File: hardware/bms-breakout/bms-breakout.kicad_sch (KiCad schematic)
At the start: 16 parts, among them J1 IN-A, J10 V-SUPP, J11 Smol_Brain_Board, J12 DE9_Socket_MountingHoles, J13 UART_CONN, J14 BMS_SW, J15 SBB_POWER, J2 IN-B, J3 IN-C, J4 BALANCE-A, J5 BALANCE-B, J6 BALANCE-C, J7 Conn_01x23, J8 BMS-OUT, J9 BMS-IN

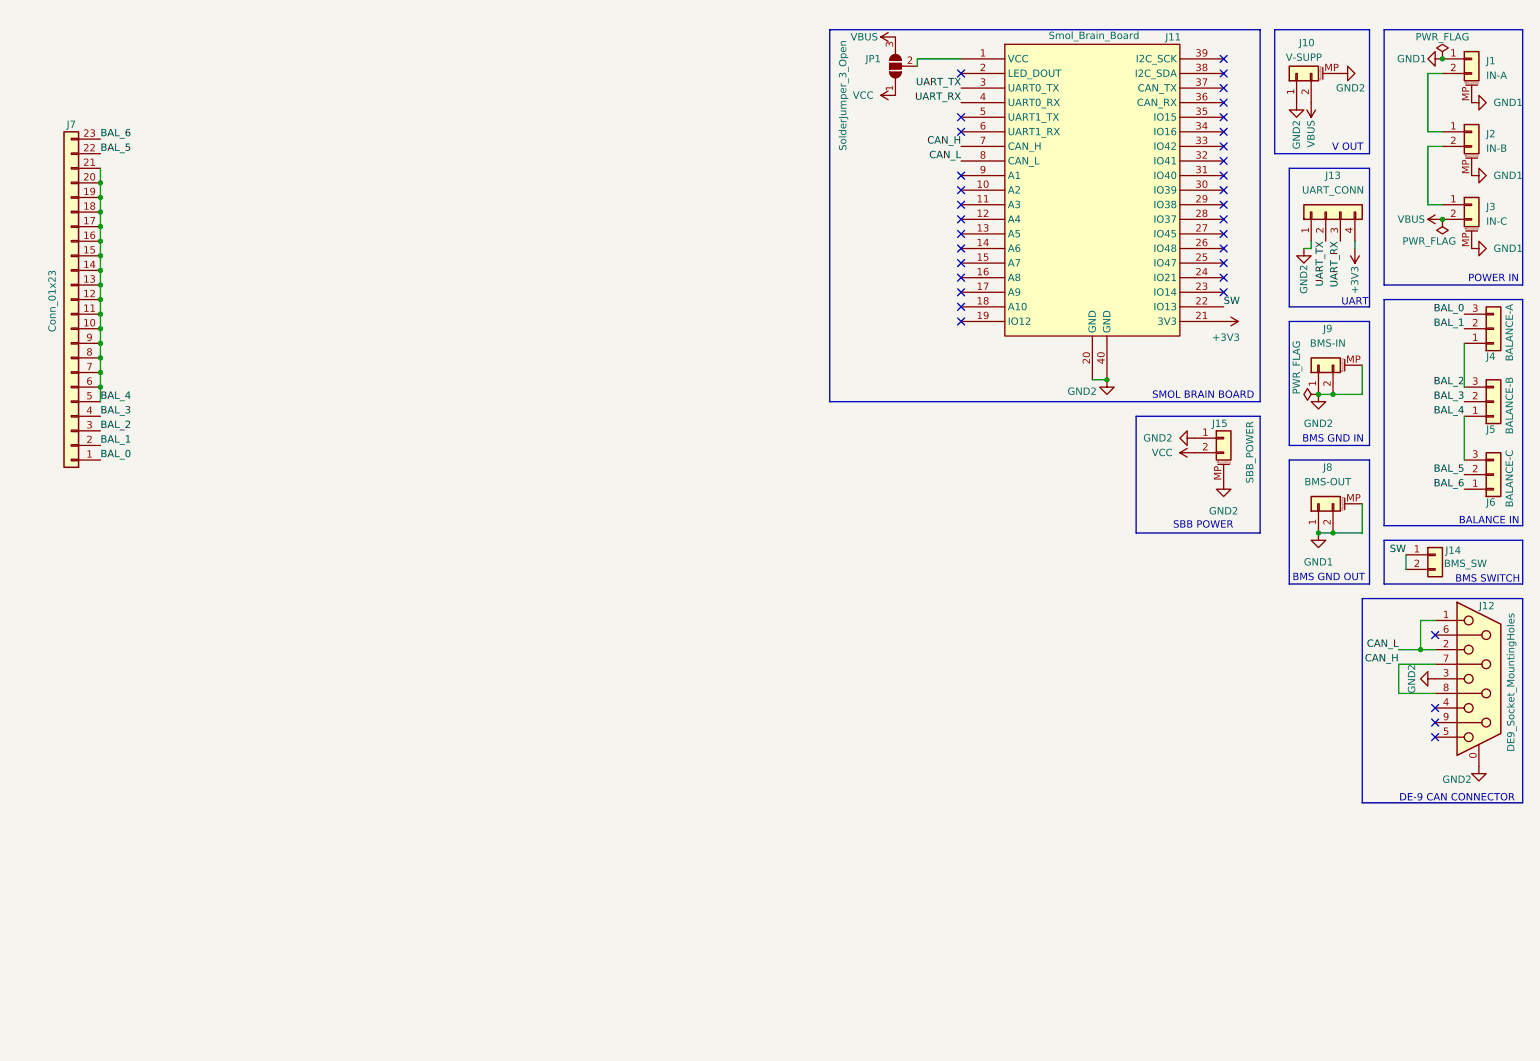
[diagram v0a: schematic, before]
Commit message: Updated Schematic
- Changed Layout
- Added Estop fet for discharge switch
- Added voltage balance connectors
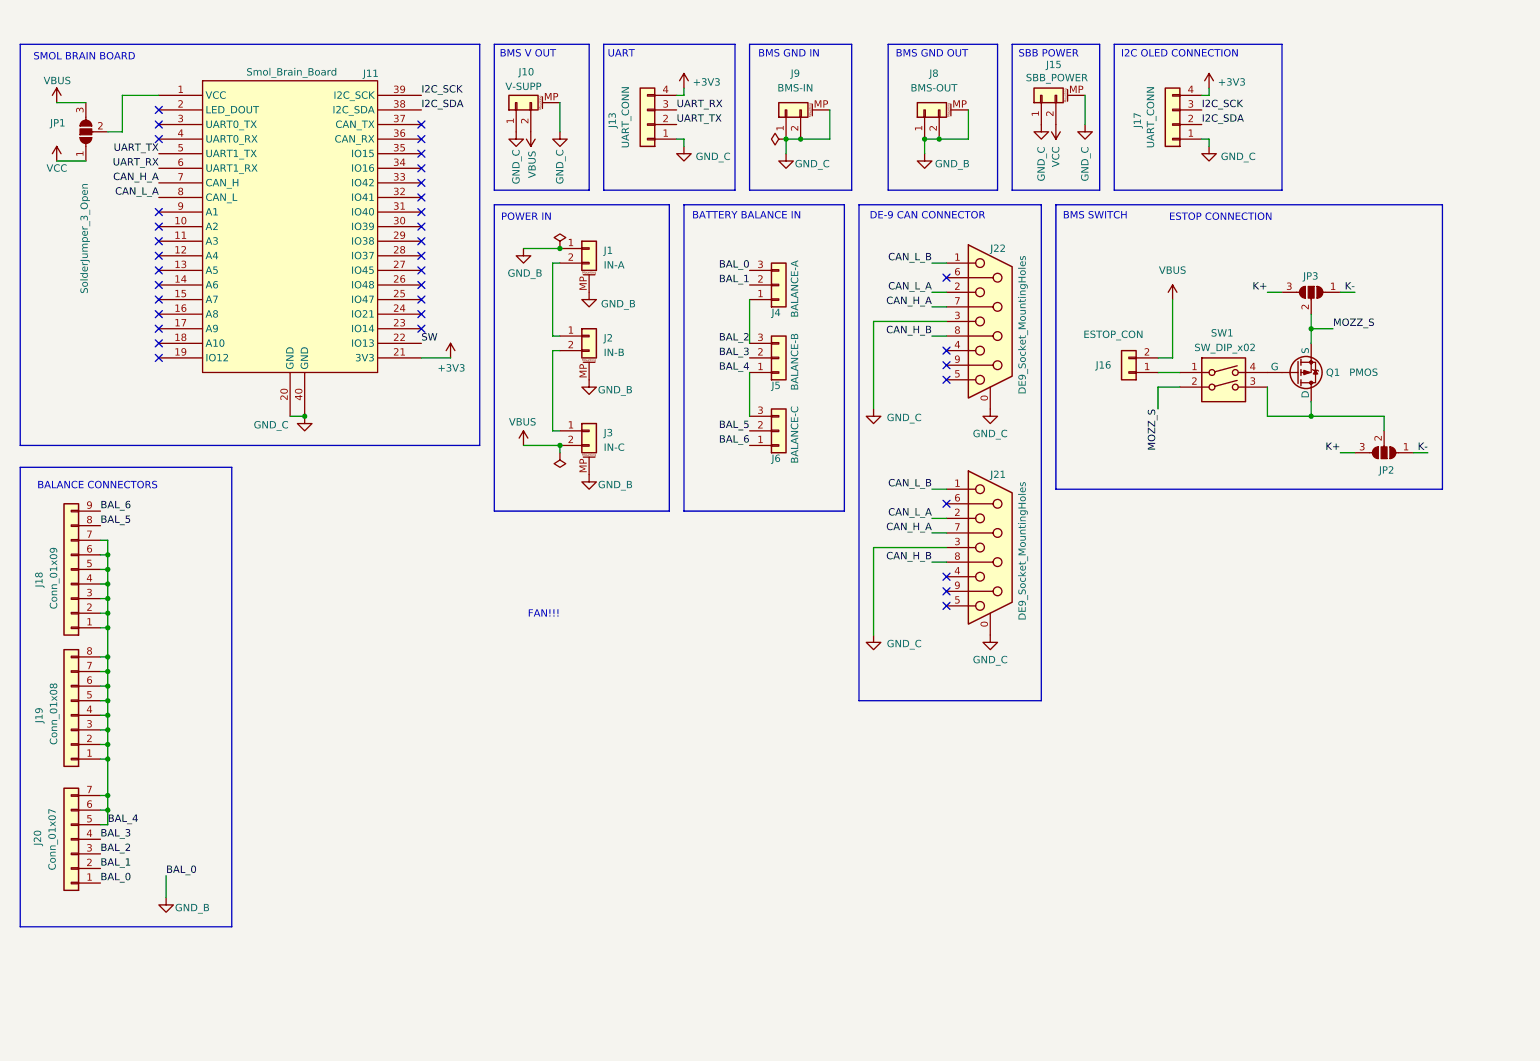
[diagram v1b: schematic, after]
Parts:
- removed J12: DE9_Socket_MountingHoles, Connector_Dsub:DSUB-9_Socket_Horizontal_P2.77x2.84mm_EdgePinOffset4.94mm_Housed_MountingHolesOffset4.94mm, symbol Connector:DE9_Socket_MountingHoles
- removed J14: BMS_SW, symbol Connector_Generic:Conn_01x02
- removed J7: Conn_01x23, symbol Connector_Generic:Conn_01x23
- added J16: ESTOP_CON, symbol Connector_Generic:Conn_01x02
- added J17: UART_CONN, Connector_JST:JST_XH_S4B-XH-A-1_1x04_P2.50mm_Horizontal, symbol Connector_Generic:Conn_01x04
- added J18: Conn_01x09, symbol Connector_Generic:Conn_01x09
- added J19: Conn_01x08, symbol Connector_Generic:Conn_01x08
- added J20: Conn_01x07, symbol Connector_Generic:Conn_01x07
- added J21, J22: DE9_Socket_MountingHoles, Connector_Dsub:DSUB-9_Socket_Horizontal_P2.77x2.84mm_EdgePinOffset4.94mm_Housed_MountingHolesOffset4.94mm, symbol Connector:DE9_Socket_MountingHoles
- added JP2, JP3: SolderJumper_3_Open, Jumper:SolderJumper-3_P2.0mm_Open_TrianglePad1.0x1.5mm, symbol Jumper:SolderJumper_3_Open
- added Q1: PMOS, symbol Simulation_SPICE:PMOS
- added SW1: SW_DIP_x02, symbol Switch:SW_DIP_x02
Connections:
- net GND1 is gone; now on net GND_B: J1.1 (Pin_1), J1.MP (MountPin), J2.MP (MountPin), J3.MP (MountPin), J8.1 (Pin_1), J8.2 (Pin_2), J8.MP (MountPin)
- net +3V3: now also J17.4 (Pin_4)
- net BAL_1: now also J20.2 (Pin_2)
- net BAL_2: now also J20.3 (Pin_3)
- net BAL_3: now also J20.4 (Pin_4)
- net BAL_4: now also J18.1 (Pin_1), J18.2 (Pin_2), J18.3 (Pin_3), J18.4 (Pin_4), J18.5 (Pin_5), J18.6 (Pin_6), J18.7 (Pin_7), J19.1 (Pin_1), J19.2 (Pin_2), J19.3 (Pin_3), J19.4 (Pin_4), J19.5 (Pin_5), J19.6 (Pin_6), J19.7 (Pin_7), J19.8 (Pin_8), J20.5 (Pin_5), J20.6 (Pin_6), J20.7 (Pin_7)
- net BAL_5: now also J18.8 (Pin_8)
- net BAL_6: now also J18.9 (Pin_9)
- net UART_RX: now also J11.6 (UART1_RX); no longer J11.4 (UART0_RX)
- net UART_TX: now also J11.5 (UART1_TX); no longer J11.3 (UART0_TX)
- net VBUS: now also J16.2 (Pin_2)
- net I2C_SDA: now reaches J11.38 (I2C_SDA)
- net I2C_SDA: now also J17.2 (Pin_2)
- net I2C_SCK: now reaches J11.39 (I2C_SCK)
- net I2C_SCK: now also J17.3 (Pin_3)
- net BAL_0 renamed GND_B
- net GND_B: now also J20.1 (Pin_1)
- net CAN_H renamed CAN_H_A
- net CAN_H_A: now also J21.7, J22.7
- net CAN_L renamed CAN_L_A
- net CAN_L_A: now also J21.2, J22.2
- net GND2 renamed GND_C
- net GND_C: now also J17.1 (Pin_1), J21.0 (PAD), J21.3, J22.0 (PAD), J22.3
- new net: J16.1 (Pin_1), SW1.1
- new net: JP2.2 (C), Q1.1 (D), SW1.3
- new net: Q1.2 (G), SW1.4
- new net CAN_H_B: J21.8, J22.8
- new net CAN_L_B: J21.1, J22.1
- new net K+: JP2.3 (B), JP3.3 (B)
- new net K-: JP2.1 (A), JP3.1 (A)
- new net MOZZ_S: JP3.2 (C), Q1.3 (S), SW1.2
- no-connect marks 35 -> 37
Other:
- note added: "BALANCE CONNECTORS"
- note added: "BATTERY BALANCE IN"
- note added: "BMS V OUT"
- note added: "ESTOP CONNECTION"
- note added: "FAN!!!"
- note added: "I2C OLED CONNECTION"
- note removed: "BALANCE IN"
- note removed: "V OUT"
- moved on the sheet: J1, J10, J11, J13, J15, J2, J3, J4, J5, J6, J8, J9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

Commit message: Started Traces
- Finished first draft of schematic
- Started first draft of traces
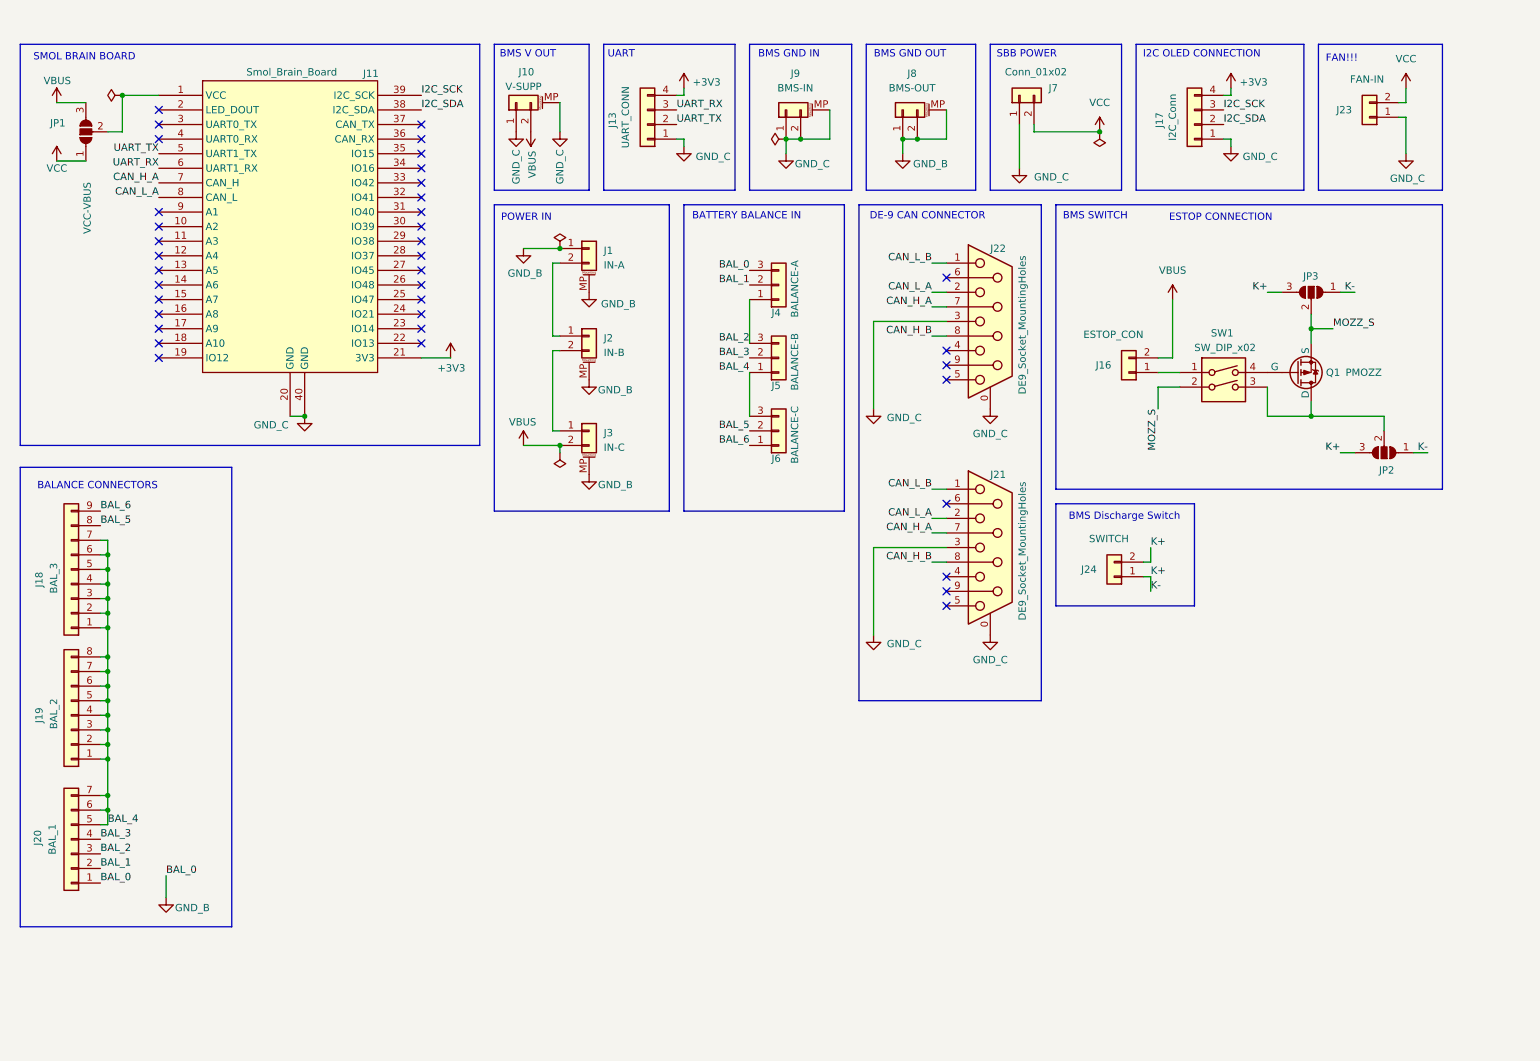
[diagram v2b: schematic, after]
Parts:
- removed J15: SBB_POWER, Connector_AMASS:AMASS_XT30PW-M_1x02_P2.50mm_Horizontal, symbol Connector_Generic_MountingPin:Conn_01x02_MountingPin
- added J23: FAN-IN, Connector_JST:JST_XH_B2B-XH-AM_1x02_P2.50mm_Vertical, symbol Connector_Generic:Conn_01x02
- added J24: SWITCH, Connector_JST:JST_XH_B2B-XH-AM_1x02_P2.50mm_Vertical, symbol Connector_Generic:Conn_01x02
- added J7: Conn_01x02, Connector_AMASS:AMASS_XT30U-M_1x02_P5.0mm_Vertical, symbol Connector_Generic:Conn_01x02
- J13: footprint Connector_JST:JST_XH_S4B-XH-A-1_1x04_P2.50mm_Horizontal -> Connector_JST:JST_XH_S4B-XH-A_1x04_P2.50mm_Horizontal
- J16: footprint (none) -> Connector_JST:JST_XH_B2B-XH-AM_1x02_P2.50mm_Vertical
- J17: value UART_CONN -> I2C_Conn; footprint Connector_JST:JST_XH_S4B-XH-A-1_1x04_P2.50mm_Horizontal -> Connector_JST:JST_XH_S4B-XH-A_1x04_P2.50mm_Horizontal
- J18: value Conn_01x09 -> BAL_3; footprint (none) -> Connector_JST:JST_XH_S9B-XH-A_1x09_P2.50mm_Horizontal
- J19: value Conn_01x08 -> BAL_2; footprint (none) -> Connector_JST:JST_XH_S8B-XH-A_1x08_P2.50mm_Horizontal
- J20: value Conn_01x07 -> BAL_1; footprint (none) -> Connector_JST:JST_XH_S7B-XH-A_1x07_P2.50mm_Horizontal
- JP1: value SolderJumper_3_Open -> VCC-VBUS; footprint Jumper:SolderJumper-3_P2.0mm_Open_TrianglePad1.0x1.5mm -> Jumper:SolderJumper-3_P1.3mm_Open_RoundedPad1.0x1.5mm
- JP2: value SolderJumper_3_Open -> Drain_Side; footprint Jumper:SolderJumper-3_P2.0mm_Open_TrianglePad1.0x1.5mm -> Jumper:SolderJumper-3_P1.3mm_Open_RoundedPad1.0x1.5mm
- JP3: value SolderJumper_3_Open -> Source_Side; footprint Jumper:SolderJumper-3_P2.0mm_Open_TrianglePad1.0x1.5mm -> Jumper:SolderJumper-3_P1.3mm_Open_RoundedPad1.0x1.5mm
- Q1: value PMOS -> PMOZZ; footprint (none) -> Package_TO_SOT_SMD:SOT-23-3
- SW1: footprint (none) -> Button_Switch_THT:SW_DIP_SPSTx02_Slide_6.7x6.64mm_W7.62mm_P2.54mm_LowProfile
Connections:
- net K- is gone; now on net K+: JP2.1 (A), JP3.1 (A)
- net GND_C: now also J23.1 (Pin_1), J7.1 (Pin_1)
- net K+: now also J24.1 (Pin_1), J24.2 (Pin_2)
- net VCC: now also J23.2 (Pin_2), J7.2 (Pin_2)
- net SW: no longer names the net of J11.22 (IO13)
- no-connect marks 37 -> 38
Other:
- note added: "BMS Discharge Switch"
- moved on the sheet: J17, J8

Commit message: Redid layout
- Redid layout
- Currently tracing board
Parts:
- removed J8: BMS-OUT, Connector_AMASS:AMASS_XT90PW-M_1x02_P10.90mm_Horizontal, symbol Connector_Generic_MountingPin:Conn_01x02_MountingPin
- removed J9: BMS-IN, Connector_AMASS:AMASS_XT90PW-M_1x02_P10.90mm_Horizontal, symbol Connector_Generic_MountingPin:Conn_01x02_MountingPin
- removed SW1: SW_DIP_x02, Button_Switch_THT:SW_DIP_SPSTx02_Slide_6.7x6.64mm_W7.62mm_P2.54mm_LowProfile, symbol Switch:SW_DIP_x02
- added H1: Mounting_1, MountingHole:MountingHole_3.2mm_M3_Pad_Via, symbol Mechanical:MountingHole_Pad
- added H2: Mounting_2, MountingHole:MountingHole_3.2mm_M3_Pad_Via, symbol Mechanical:MountingHole_Pad
- added H3: Mounting_3, MountingHole:MountingHole_3.2mm_M3_Pad_Via, symbol Mechanical:MountingHole_Pad
- added H5, H6: BMS_OUT, MountingHole:MountingHole_3.5mm_Pad_Via, symbol Mechanical:MountingHole_Pad
- added H7, H8: BMS_IN, MountingHole:MountingHole_3.5mm_Pad_Via, symbol Mechanical:MountingHole_Pad
- added JP4: Mozz_Jumper, Jumper:SolderJumper-2_P1.3mm_Open_RoundedPad1.0x1.5mm, symbol Jumper:Jumper_2_Open
- added SW2: Kill_Switch, Button_Switch_THT:SW_DIP_SPSTx01_Slide_6.7x4.1mm_W7.62mm_P2.54mm_LowProfile, symbol Switch:SW_SPST
- J7: footprint Connector_AMASS:AMASS_XT30U-M_1x02_P5.0mm_Vertical -> Connector_AMASS:AMASS_XT30PW-M_1x02_P2.50mm_Horizontal
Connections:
- net GND_B: now also H7.1, H8.1; no longer J1.MP (MountPin), J2.MP (MountPin), J3.MP (MountPin)
- net GND_C: now also H1.1, H2.1, H5.1, H6.1; no longer J10.MP (MountPin)
- net MOZZ_S: now also JP4.1 (A)
- net BAT2-3: now reaches J2.2 (Pin_2), J3.1 (Pin_1)
- net at J16.1 (Pin_1): now also SW2.1 (A)
- net at JP2.2 (C), Q1.1 (D): now also JP4.2 (B)
- net at Q1.2 (G): now also SW2.2 (B)
- net BAT1-2: now reaches J1.2 (Pin_2), J2.1 (Pin_1)
- net K+ renamed K_NEG
- net K_NEG: no longer J24.2 (Pin_2), JP2.3 (B), JP3.3 (B)
- new net K_POS: J24.2 (Pin_2), JP2.3 (B), JP3.3 (B)
- no-connect marks 38 -> 43
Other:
- note added: "Mounting Hole"

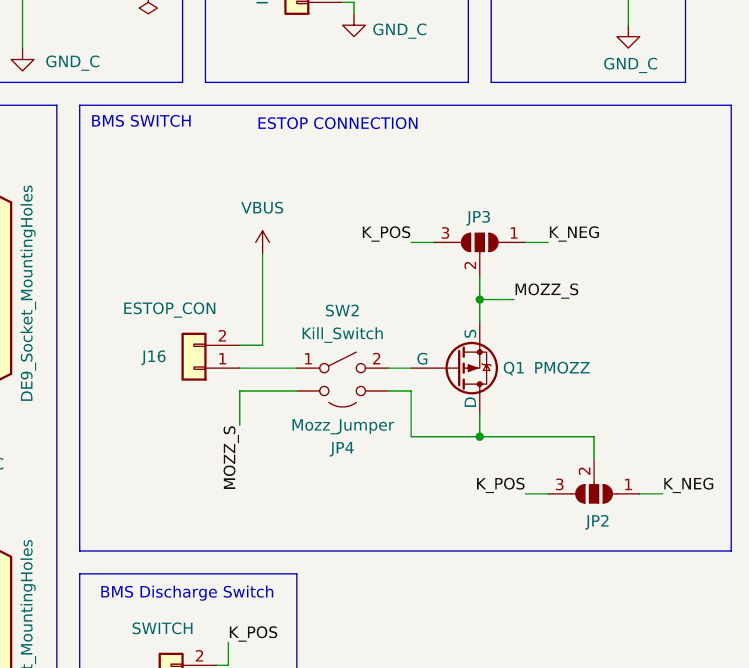
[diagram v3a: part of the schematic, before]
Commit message: Almost finished tracing BMS
- Updated GND planes
- CAN Traces almost done
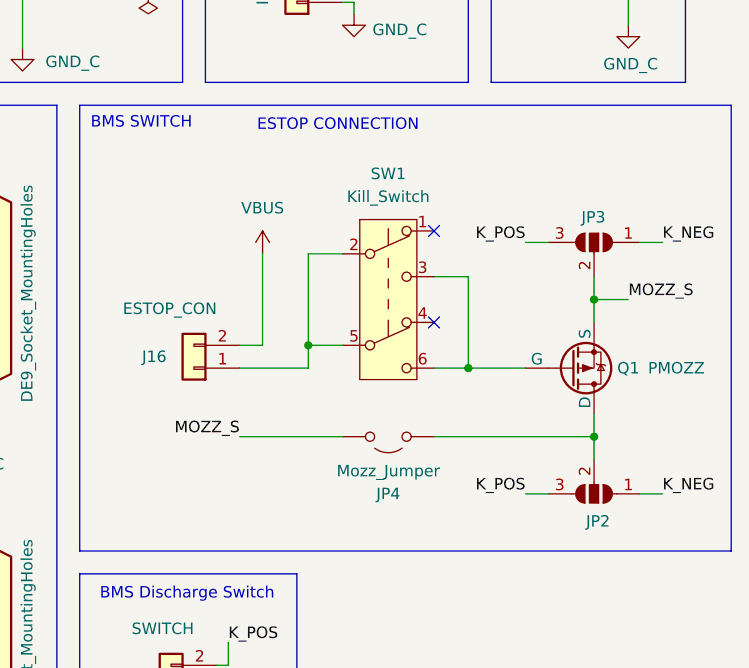
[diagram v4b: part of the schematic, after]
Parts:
- removed SW2: Kill_Switch, Button_Switch_THT:SW_DIP_SPSTx01_Slide_6.7x4.1mm_W7.62mm_P2.54mm_LowProfile, symbol Switch:SW_SPST
- added SW1: Kill_Switch, Button_Switch_THT:SW_CK_JS202011CQN_DPDT_Straight, symbol Switch:SW_Push_DPDT
- J16, J23, J24: footprint Connector_JST:JST_XH_B2B-XH-AM_1x02_P2.50mm_Vertical -> Connector_JST:JST_XH_B2B-XH-A_1x02_P2.50mm_Vertical
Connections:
- net at J16.1 (Pin_1): now also SW1.2 (B), SW1.5 (B)
- net at Q1.2 (G): now also SW1.3 (C), SW1.6 (C)
- no-connect marks 43 -> 45
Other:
- moved on the sheet: JP3, JP4, Q1
